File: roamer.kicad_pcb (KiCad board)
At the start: 4 copper layers, 100 parts, among them J1 Conn_Coaxial_Small, J2 JSTPH, J3 Conn_02x05_Odd_Even, J4 Conn_Coaxial_Small, J8 MEM2075-00-140-01-A, Q3 DMP2070UQ-7, SW1 KMR2, U1 2MB Flash, U2 AP2112K-3.3, U3 MCP73831-2-OT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

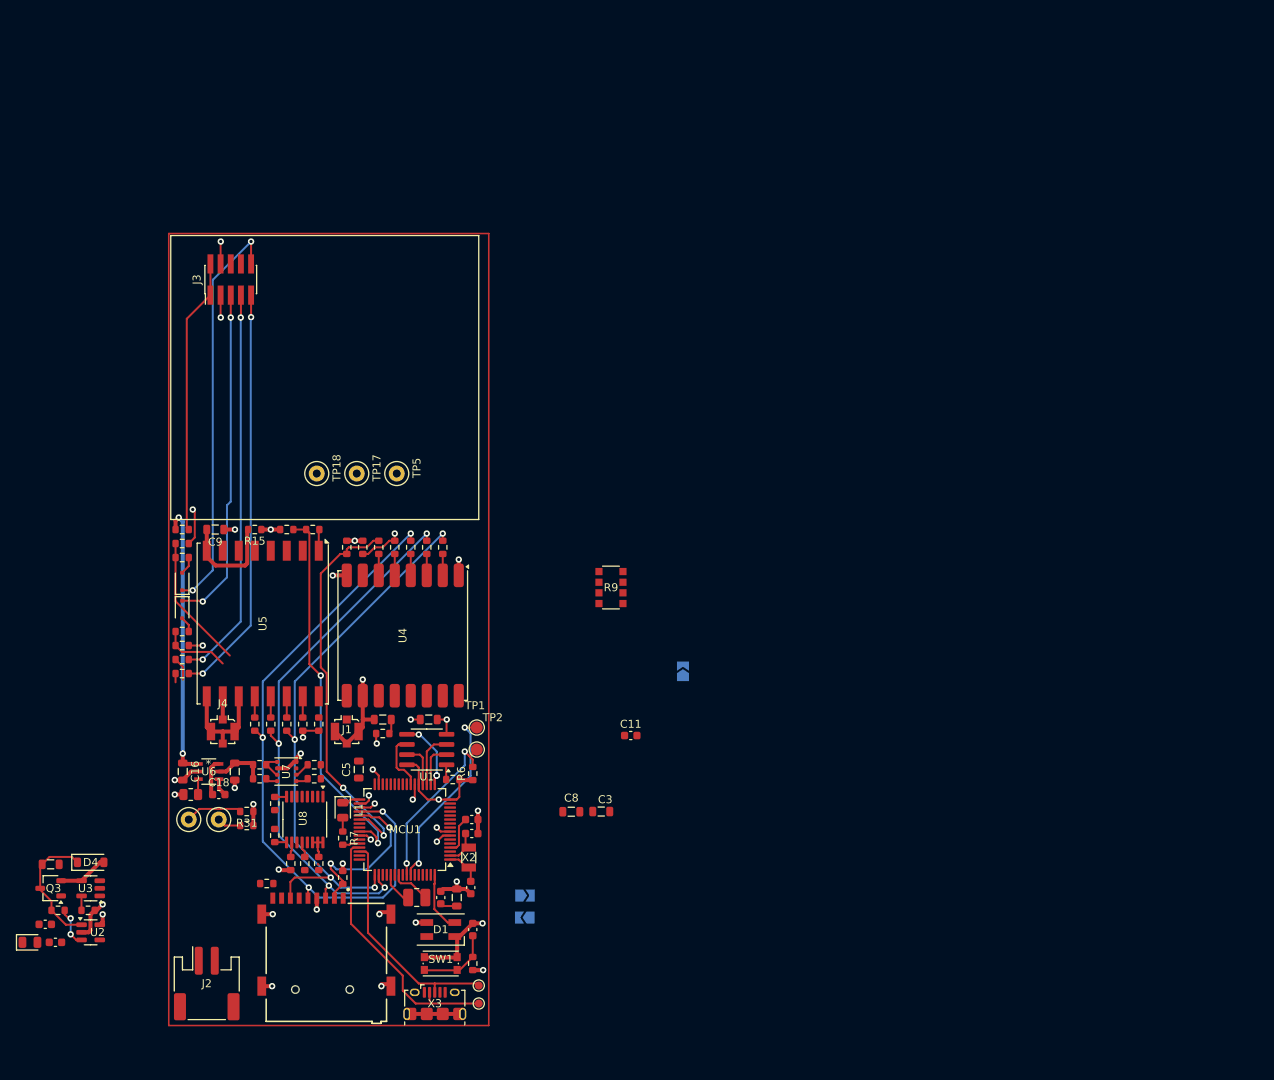
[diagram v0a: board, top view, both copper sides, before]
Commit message: Redid board layout. Still have to add bypass caps
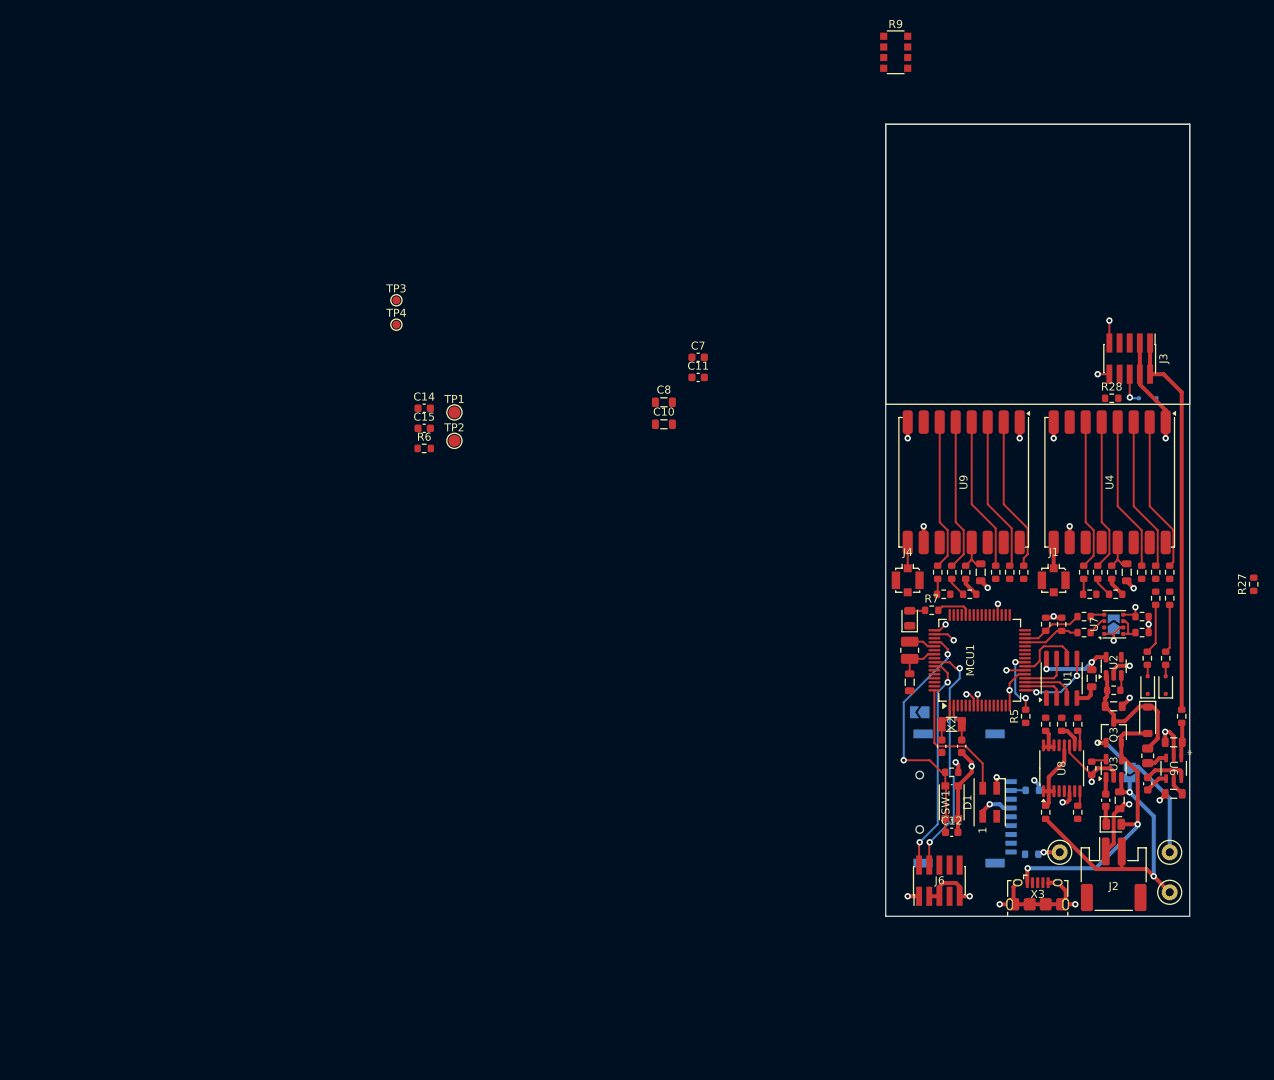
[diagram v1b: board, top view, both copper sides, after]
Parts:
- removed the D2 at (205.6, 125.2)
- removed TP16, TP17, TP18, TP5, TP6: TestPoint, TestPoint:TestPoint_Loop_D2.50mm_Drill1.0mm
- removed U5: RFM69W, RF_Module:HOPERF_RFM69HW
- added D2: 1N4148, Diode_SMD:D_SOD-323F, F.Cu at (326.2, 134.6)
- added D2: 1N4148, Diode_SMD:D_SOD-323F, B.Cu at (326.2, 98.8)
- added J6: Conn_02x05_Odd_Even, Connector_PinHeader_1.27mm:PinHeader_2x05_P1.27mm_Vertical_SMD, F.Cu at (300.2, 159.1)
- added TP7: TestPoint, TestPoint:TestPoint_Loop_D2.50mm_Drill1.0mm, F.Cu at (315.2, 155.5)
- added TP8: TestPoint, TestPoint:TestPoint_Loop_D2.50mm_Drill1.0mm, F.Cu at (329.0, 160.5)
- added TP9: TestPoint, TestPoint:TestPoint_Loop_D2.50mm_Drill1.0mm, F.Cu at (329.0, 155.5)
- added U9: RFM96W-433S2, RF_Module:HOPERF_RFM9XW_SMD, F.Cu at (303.2, 109.2)
- J8, R23, R34: moved to B.Cu
- moved CHG1 136.3 mm to (322.0, 152.0)
- moved R3 134.8 mm to (322.0, 135.2)
- moved C6 134.3 mm to (322.0, 137.2)
- moved Q3 134.3 mm to (322.0, 140.5), turned to 90 degrees
- moved R27 134.3 mm to (339.5, 122.0), turned to 90 degrees
- moved D4 133.3 mm to (326.2, 139.0), turned to -90 degrees
- moved R2 132.5 mm to (321.0, 149.0), turned to -90 degrees
- moved U2 132.1 mm to (322.0, 132.2), turned to 90 degrees
- moved U3 128.8 mm to (322.0, 145.0), turned to 90 degrees
- moved R41 127.1 mm to (330.5, 138.5), turned to 90 degrees
- moved R4 126.7 mm to (319.2, 145.0), turned to 90 degrees
- moved C16 123.9 mm to (329.5, 141.8), turned to 180 degrees
- moved R40 123.6 mm to (329.0, 123.8), turned to -90 degrees
- moved D3 123.6 mm to (328.5, 134.6)
- moved R42 123.6 mm to (328.5, 131.2), turned to -90 degrees
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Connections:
- C17 pad 1: +3V3 -> /Power - Management/POWER_IN
- C6 pad 1: Net-(D4-K) -> /Power - Management/POWER_IN
- D4 pad 1: Net-(D4-K) -> /Power - Management/POWER_IN
- J3 pad 10: Net-(D3-K) -> Net-(J3-Pin_10)
- J3 pad 5: Net-(D2-K) -> unconnected-(J3-Pin_5-Pad5)
- J3 pad 6: unconnected-(J3-Pin_6-Pad6) -> Net-(D2-K)
- J3 pad 7: Net-(J3-Pin_7) -> unconnected-(J3-Pin_7-Pad7)
- J3 pad 8: unconnected-(J3-Pin_8-Pad8) -> Net-(J3-Pin_8)
- J3 pad 9: Net-(J3-Pin_9) -> Net-(D3-K)
- Q3 pad 3: Net-(D4-K) -> /Power - Management/POWER_IN
- R27 pad 1: Net-(J3-Pin_7) -> Net-(J3-Pin_10)
- R28 pad 1: Net-(J3-Pin_9) -> /Bus - I2C/I2C.SCL
- R28 pad 2: /Bus - I2C/I2C.SCL -> Net-(J3-Pin_8)
- R3 pad 1: Net-(D4-K) -> /Power - Management/POWER_IN
- R38 pad 2: +3V3 -> /Power - Management/POWER_IN
- U2 pad 1: Net-(D4-K) -> /Power - Management/POWER_IN
- U6 pad 5: +3V3 -> /Power - Management/POWER_IN
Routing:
- net /Bus - SPI/SPI.SCK: track 82.7 -> 1.34 mm, vias 4 -> 1
- net /Bus - SPI/SPI.MISO: track 69.8 -> 1.70 mm, vias 4 -> 1
- net /Bus - SPI/SPI.MOSI: track 68.5 -> 2.72 mm, vias 4 -> 1
- net Net-(J3-Pin_9): track 51.6 -> 0.00 mm, vias 2 -> 0
- net Net-(J3-Pin_7): track 49.3 -> 0.00 mm, vias 2 -> 0
- net Net-(D3-K): track 51.0 -> 2.86 mm, vias 2 -> 1
- net /Comms - LoRa 900/~{RESET_LORA_900}: track 49.1 -> 1.96 mm, vias 2 -> 0
- net /Comms - LoRa 433/~{RESET_LORA_433}: track 47.8 -> 1.71 mm, vias 2 -> 0
- net Net-(D2-K): track 42.4 -> 3.96 mm, vias 2 -> 1
- net +BATT: track 0.00 -> 37.7 mm, vias 0 -> 2
- net /Interface - uUSB/D-: track 32.7 -> 0.00 mm
- net +5V: track 34.8 -> 4.72 mm, vias 2 -> 0
- net VBUS: track 6.29 -> 36.2 mm, vias 0 -> 2
- net /Interface - uUSB/D+: track 28.7 -> 0.00 mm
- net /MCU/~{RESET}: track 9.05 -> 31.6 mm, vias 0 -> 2
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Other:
- board outline added: 38 x 99 mm

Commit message: Connected all signals except Buses
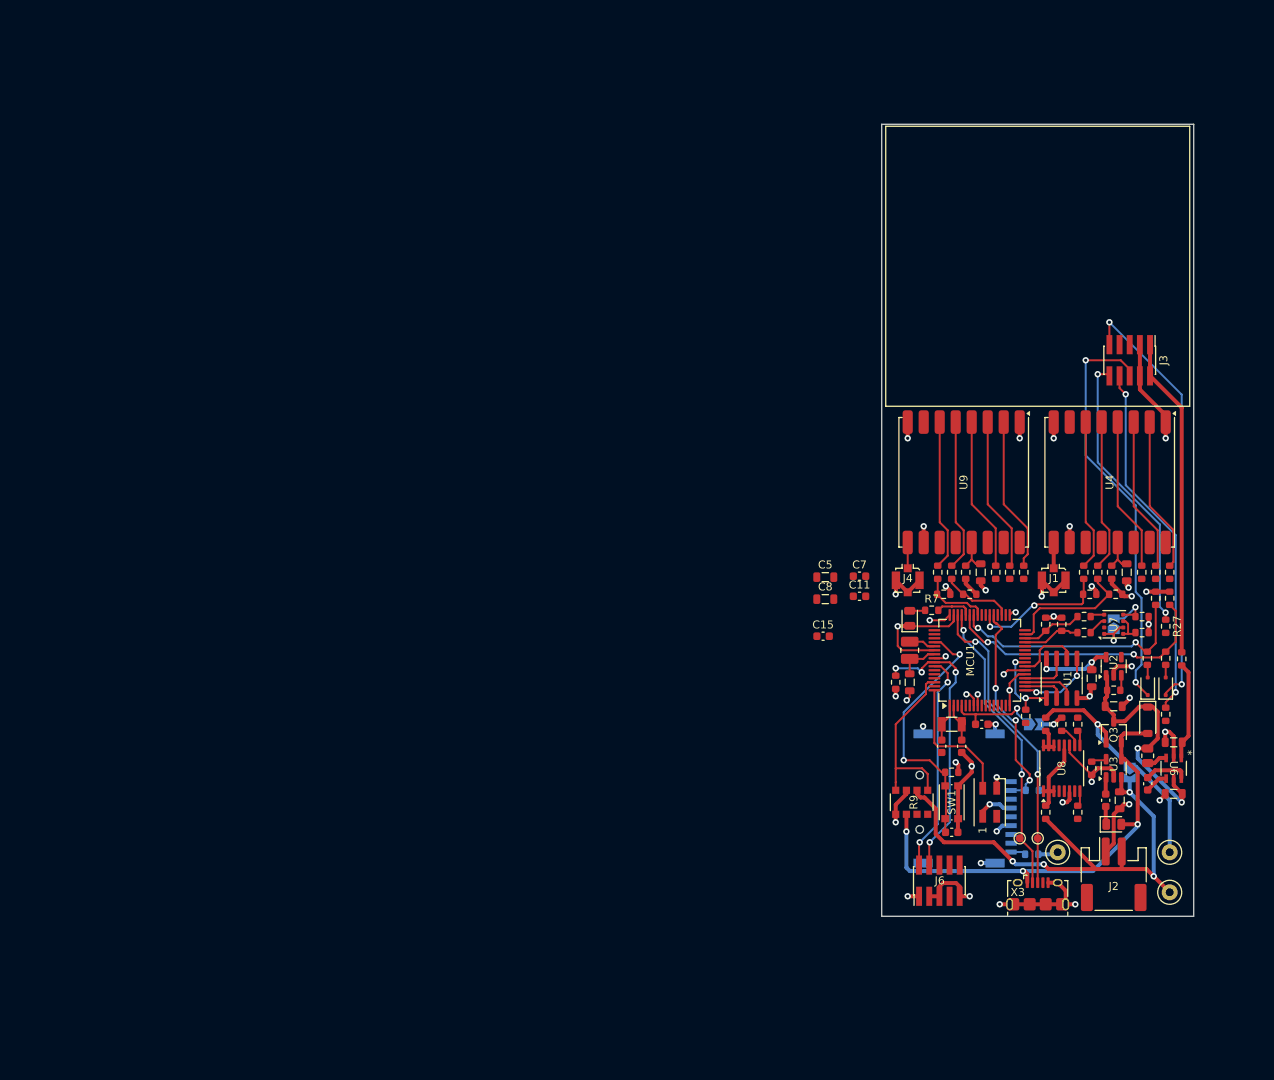
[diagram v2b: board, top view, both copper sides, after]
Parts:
- removed the D2 at (326.2, 134.6)
- removed the D2 at (326.2, 98.8)
- removed TP1, TP2: TestPoint, TestPoint:TestPoint_Pad_D1.5mm
- added D2: 1N4148, Diode_SMD:D_SOD-323F, F.Cu at (326.2, 134.8)
- moved TP3 104.6 mm to (312.5, 153.8)
- moved TP4 101.0 mm to (310.2, 153.8)
- moved R9 93.8 mm to (296.8, 149.2), turned to -90 degrees
- moved C14 80.1 mm to (305.5, 139.5)
- moved R6 65.8 mm to (294.8, 134.2), turned to 90 degrees
- moved C10 62.2 mm to (319.2, 133.8), turned to -90 degrees
- moved C15 56.2 mm to (285.7, 128.5)
- moved R28 40.1 mm to (328.5, 138.2), turned to 90 degrees
- moved C5 35.6 mm to (285.9, 121.1), turned to 0 degrees
- moved C11 34.0 mm to (290.2, 123.5)
- moved C7 34.0 mm to (290.2, 121.0)
- moved C8 31.8 mm to (285.9, 123.9)
- moved JP1 14.3 mm to (312.0, 139.5), turned to 0 degrees
- moved R27 12.2 mm to (328.5, 127.2), turned to -90 degrees
- moved R41 7.18 mm to (330.5, 131.3)
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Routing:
- net Net-(D3-K): track 2.86 -> 54.5 mm, vias 1 -> 2
- net Net-(D2-K): track 3.96 -> 52.5 mm, vias 1 -> 2
- net Net-(J3-Pin_8): track 0.00 -> 44.9 mm, vias 0 -> 2
- net /Interface - uUSB/D+: track 0.00 -> 38.6 mm, vias 0 -> 2
- net GND: track 104.8 -> 142.6 mm, vias 24 -> 34
- net /Interface - uUSB/D-: track 0.00 -> 37.2 mm, vias 0 -> 2
- net Net-(J3-Pin_10): track 1.71 -> 35.9 mm, vias 1 -> 2
- net +BATT: track 37.7 -> 66.7 mm, vias 2 -> 4
- net /MCU/AIRQ_SET: track 6.06 -> 34.6 mm, vias 0 -> 2
- net /Interface - uSD/CS_uSD: track 2.12 -> 27.1 mm, vias 0 -> 3
- net /MCU/~{AIRQ_RESET}: track 6.28 -> 31.1 mm, vias 0 -> 2
- net Net-(MCU1-PB01): track 0.00 -> 22.3 mm
- net VBUS: track 36.2 -> 58.3 mm, vias 2 -> 3
- net /Comms - LoRa 900/~{RESET_LORA_900}: track 1.96 -> 17.3 mm, vias 0 -> 2
- net +3V3: track 35.5 -> 50.5 mm, vias 10 -> 17
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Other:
- board size 38 x 99 mm -> 39 x 99 mm

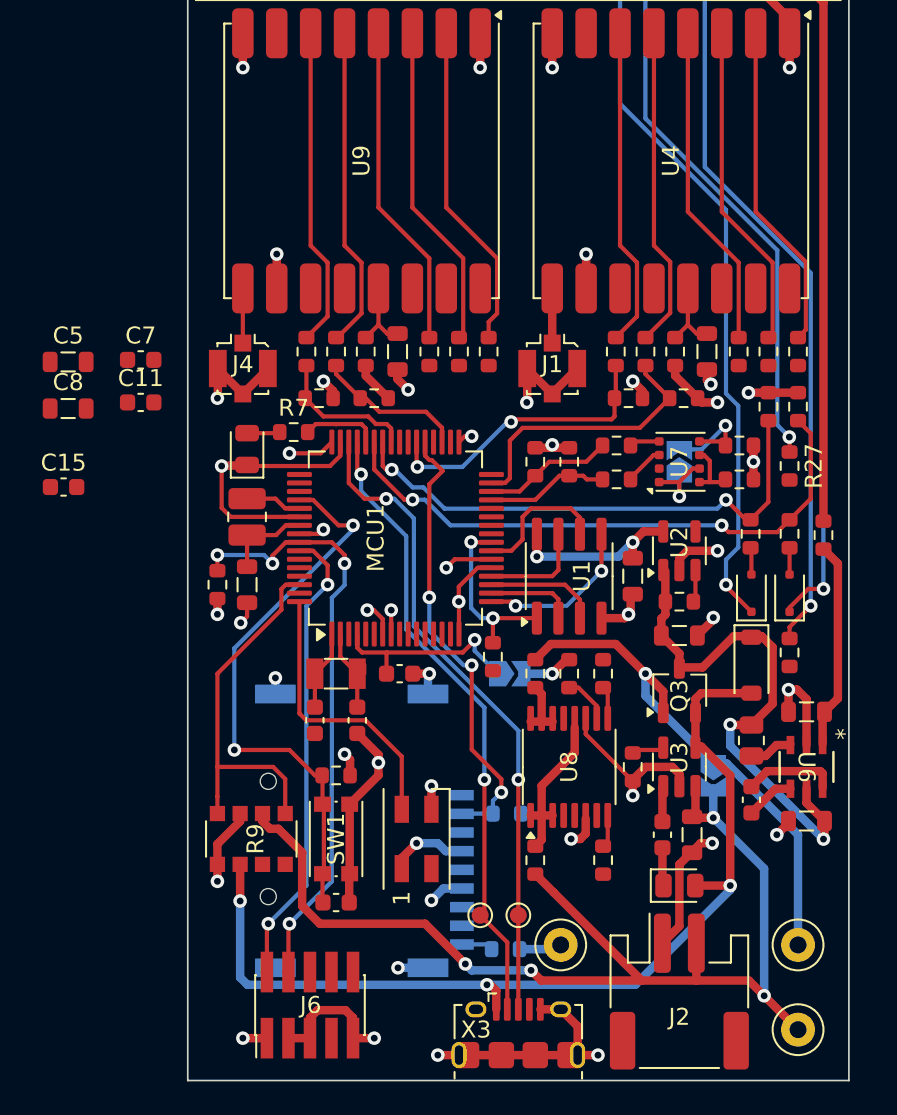
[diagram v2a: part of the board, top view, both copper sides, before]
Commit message: Connected all signal lines
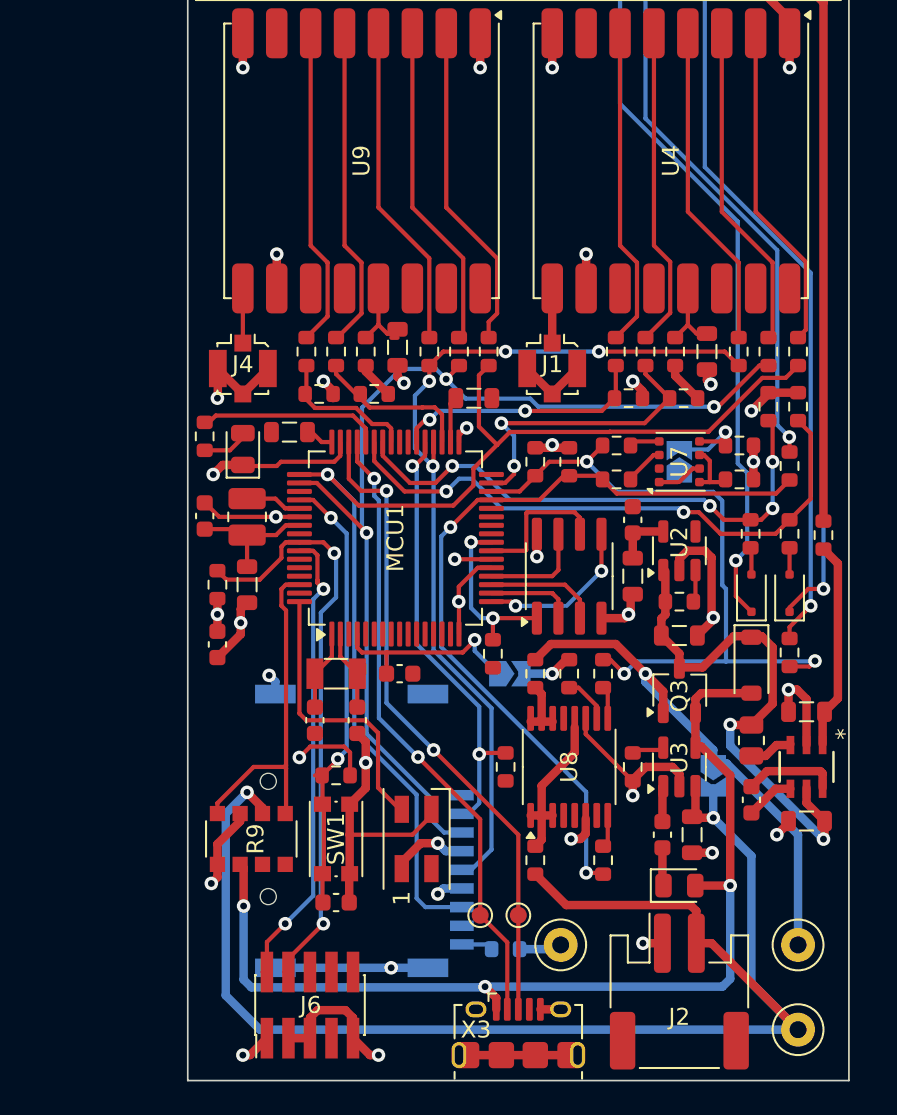
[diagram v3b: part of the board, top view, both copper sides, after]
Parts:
- R23: moved to F.Cu
- moved C7 30.5 mm to (319.2, 130.4), turned to 90 degrees
- moved C5 24.0 mm to (309.9, 123.2)
- moved C11 15.0 mm to (294.8, 137.8), turned to 90 degrees
- moved C8 13.1 mm to (299.0, 125.2), turned to 180 degrees
- moved C15 8.50 mm to (294.0, 130.2), turned to -90 degrees
- moved R7 5.26 mm to (294.0, 125.5), turned to 90 degrees
- moved R23 2.76 mm to (311.8, 145.0), turned to 90 degrees
- moved C9 0.25 mm to (305.4, 120.2)
- moved L1 0.25 mm to (296.2, 126.2)
- moved R36 0.25 mm to (304.0, 123.0)
- moved R44 0.25 mm to (300.8, 123.0)
- moved R5 0.18 mm to (311.0, 138.3)
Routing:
- net /Bus - SPI/SPI.MISO: track 0.00 -> 70.1 mm, vias 0 -> 1
- net /Bus - SPI/SPI.MOSI: track 0.00 -> 61.6 mm, vias 0 -> 3
- net /Bus - SPI/SPI.SCK: track 0.00 -> 54.0 mm, vias 0 -> 4
- net /Bus - I2C/I2C.SDA: track 7.24 -> 47.5 mm, vias 0 -> 2
- net /Bus - I2C/I2C.SCL: track 7.68 -> 41.0 mm, vias 0 -> 3
- net +BATT: track 66.7 -> 88.6 mm, vias 4 -> 2
- net /MCU/~{RESET}: track 33.3 -> 26.5 mm
- net Net-(MCU1-PA23): track 4.54 -> 10.5 mm
- net +3V3: track 50.5 -> 46.7 mm, vias 17 -> 12
- net VBUS: track 58.3 -> 61.3 mm
- net GND: track 142.6 -> 139.7 mm, vias 34 -> 28
- net Net-(MCU1-VSW): track 5.19 -> 7.94 mm
- net /Comms - LoRa 900/~{RESET_LORA_900}: track 17.3 -> 15.2 mm
- net Net-(MCU1-PB01): track 22.3 -> 20.3 mm
- net /Comms - LoRa 900/CS_LORA_900: track 16.4 -> 17.9 mm, vias 0 -> 2
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
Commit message: Finished layout
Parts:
- R34: moved to F.Cu
- moved R34 81.1 mm to (232.8, 174.0), turned to 0 degrees
- moved R24 78.1 mm to (242.5, 144.7)
- moved R25 78.0 mm to (242.5, 146.5)
- moved C11 78.0 mm to (219.0, 156.2)
- moved C13 78.0 mm to (220.8, 152.7)
- moved L2 78.0 mm to (220.8, 148.7)
- moved R6 78.0 mm to (219.0, 152.7)
- moved R26 77.7 mm to (250.0, 146.5)
- moved R29 77.7 mm to (250.0, 144.5)
- moved C1 77.7 mm to (248.1, 138.9)
- moved C10 77.7 mm to (243.8, 152.2)
- moved C12 77.7 mm to (226.2, 171.4)
- moved C14 77.7 mm to (230.0, 157.9)
- moved C15 77.7 mm to (218.5, 148.6)
- moved C16 77.7 mm to (254.0, 160.2)
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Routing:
- net GND: track 139.7 -> 166.7 mm, vias 28 -> 34
- net +3V3: track 46.7 -> 71.5 mm, vias 12 -> 16
- net /Comms - LoRa 900/CS_LORA_900: track 17.9 -> 19.2 mm
- net unconnected-(J8-CD-PadP9): track 1.87 -> 2.95 mm, vias 0 -> 1
- net /Bus - SPI/SPI.MOSI: track 61.6 -> 62.4 mm
- net /Bus - SPI/SPI.MISO: track 70.1 -> 69.4 mm
- net Net-(D3-K): track 54.5 -> 55.1 mm
- net Net-(J3-Pin_8): track 44.9 -> 45.4 mm
- net VBUS: track 61.3 -> 60.7 mm
- net Net-(MCU1-VSW): track 7.94 -> 8.44 mm
